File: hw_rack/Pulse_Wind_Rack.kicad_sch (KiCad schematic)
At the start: 12 parts, among them J1 PH2.00, J2 PH2.00, J3 AudioJack4, U1 ME6206A33XG

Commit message: fw: Rack board? To be revised
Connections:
- net GND: now also J1.1 (Pin_1); no longer J1.2 (Pin_2)
- net V+: now also J1.2 (Pin_2); no longer J1.1 (Pin_1)
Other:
- moved on the sheet: J2
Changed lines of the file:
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@@
 	(symbol
 		(lib_id "power:GND")
-		(at 48.26 38.1 90)
+		(at 48.26 35.56 90)
 		(unit 1)
 		(exclude_from_sim no)
@@
 		(fields_autoplaced yes)
 		(property "Reference" "#PWR02"
-			(at 54.61 38.1 0)
+			(at 54.61 35.56 0)
 			(effects
 				(font
@@
 		)
 		(property "Value" "GND"
-			(at 53.34 38.1 0)
+			(at 53.34 35.56 0)
 			(effects
 				(font
@@
 		)
 		(property "Footprint" ""
-			(at 48.26 38.1 0)
+			(at 48.26 35.56 0)
 			(effects
 				(font
@@
 		)
 		(property "Datasheet" ""
-			(at 48.26 38.1 0)
+			(at 48.26 35.56 0)
 			(effects
 				(font
@@
 		)
 		(property "Description" "Power symbol creates a global label with name \"GND\" , ground"
-			(at 48.26 38.1 0)
+			(at 48.26 35.56 0)
 			(effects
 				(font
@@
 	(symbol
 		(lib_id "Connector_Generic_MountingPin:Conn_01x02_MountingPin")
-		(at 69.85 35.56 0)
-		(unit 1)
-		(exclude_from_sim no)
-		(in_bom yes)
-		(on_board yes)
-		(dnp no)
-		(fields_autoplaced yes)
+		(at 69.85 38.1 0)
+		(mirror x)
+		(unit 1)
+		(exclude_from_sim no)
+		(in_bom yes)
+		(on_board yes)
+		(dnp no)
 		(property "Reference" "J2"
-			(at 69.85 29.21 0)
+			(at 69.85 44.45 0)
 			(effects
 				(font
@@
 		)
 		(property "Value" "PH2.00"
-			(at 69.85 31.75 0)
+			(at 69.85 41.91 0)
 			(effects
 				(font
@@
 		)
 		(property "Footprint" "Connector_JST:JST_PH_S2B-PH-SM4-TB_1x02-1MP_P2.00mm_Horizontal"
-			(at 69.85 35.56 0)
+			(at 69.85 38.1 0)
 			(effects
 				(font
@@
 		)
 		(property "Datasheet" "~"
-			(at 69.85 35.56 0)
+			(at 69.85 38.1 0)
 			(effects
 				(font
@@
 		)
 		(property "Description" "Generic connectable mounting pin connector, single row, 01x02, script generated (kicad-library-utils/schlib/autogen/connector/)"
-			(at 69.85 35.56 0)
+			(at 69.85 38.1 0)
 			(effects
 				(font
@@
 	(symbol
 		(lib_id "power:+BATT")
-		(at 64.77 35.56 90)
+		(at 64.77 38.1 90)
 		(mirror x)
 		(unit 1)
@@
 		(fields_autoplaced yes)
 		(property "Reference" "#PWR05"
-			(at 68.58 35.56 0)
+			(at 68.58 38.1 0)
 			(effects
 				(font
@@
 		)
 		(property "Value" "V+"
-			(at 60.96 35.5599 90)
+			(at 60.96 38.0999 90)
 			(effects
 				(font
@@
 		)
 		(property "Footprint" ""
-			(at 64.77 35.56 0)
+			(at 64.77 38.1 0)
 			(effects
 				(font
@@
 		)
 		(property "Datasheet" ""
-			(at 64.77 35.56 0)
+			(at 64.77 38.1 0)
 			(effects
 				(font
@@
 		)
 		(property "Description" "Power symbol creates a global label with name \"+BATT\""
-			(at 64.77 35.56 0)
+			(at 64.77 38.1 0)
 			(effects
 				(font
@@
 	(symbol
 		(lib_id "power:GND")
-		(at 64.77 38.1 270)
+		(at 64.77 35.56 270)
 		(mirror x)
 		(unit 1)
@@
 		(fields_autoplaced yes)
 		(property "Reference" "#PWR06"
-			(at 58.42 38.1 0)
+			(at 58.42 35.56 0)
 			(effects
 				(font
@@
 		)
 		(property "Value" "GND"
-			(at 59.69 38.1 0)
+			(at 59.69 35.56 0)
 			(effects
 				(font
@@
 		)
 		(property "Footprint" ""
-			(at 64.77 38.1 0)
+			(at 64.77 35.56 0)
 			(effects
 				(font
@@
 		)
 		(property "Datasheet" ""
-			(at 64.77 38.1 0)
+			(at 64.77 35.56 0)
 			(effects
 				(font
@@
 		)
 		(property "Description" "Power symbol creates a global label with name \"GND\" , ground"
-			(at 64.77 38.1 0)
+			(at 64.77 35.56 0)
 			(effects
 				(font
@@
 	(symbol
 		(lib_id "power:+BATT")
-		(at 48.26 35.56 270)
+		(at 48.26 38.1 270)
 		(unit 1)
 		(exclude_from_sim no)
@@
 		(fields_autoplaced yes)
 		(property "Reference" "#PWR03"
-			(at 44.45 35.56 0)
+			(at 44.45 38.1 0)
 			(effects
 				(font
@@
 		)
 		(property "Value" "V+"
-			(at 52.07 35.5599 90)
+			(at 52.07 38.0999 90)
 			(effects
 				(font
@@
 		)
 		(property "Footprint" ""
-			(at 48.26 35.56 0)
+			(at 48.26 38.1 0)
 			(effects
 				(font
@@
 		)
 		(property "Datasheet" ""
-			(at 48.26 35.56 0)
+			(at 48.26 38.1 0)
 			(effects
 				(font
@@
 		)
 		(property "Description" "Power symbol creates a global label with name \"+BATT\""
-			(at 48.26 35.56 0)
+			(at 48.26 38.1 0)
 			(effects
 				(font
@@
 	(symbol
 		(lib_id "power:GND")
-		(at 69.85 43.18 0)
-		(mirror y)
+		(at 69.85 30.48 0)
+		(mirror x)
 		(unit 1)
 		(exclude_from_sim no)
@@
 		(fields_autoplaced yes)
 		(property "Reference" "#PWR04"
-			(at 69.85 49.53 0)
+			(at 69.85 24.13 0)
 			(effects
 				(font
@@
 		)
 		(property "Value" "GND"
-			(at 69.85 48.26 0)
+			(at 69.85 25.4 0)
 			(effects
 				(font
@@
 		)
 		(property "Footprint" ""
-			(at 69.85 43.18 0)
+			(at 69.85 30.48 0)
 			(effects
 				(font
@@
 		)
 		(property "Datasheet" ""
-			(at 69.85 43.18 0)
+			(at 69.85 30.48 0)
 			(effects
 				(font
@@
 		)
 		(property "Description" "Power symbol creates a global label with name \"GND\" , ground"
-			(at 69.85 43.18 0)
-			(effects
-				(font
+			(at 69.85 30.48 0)
+			(effects
+				(font

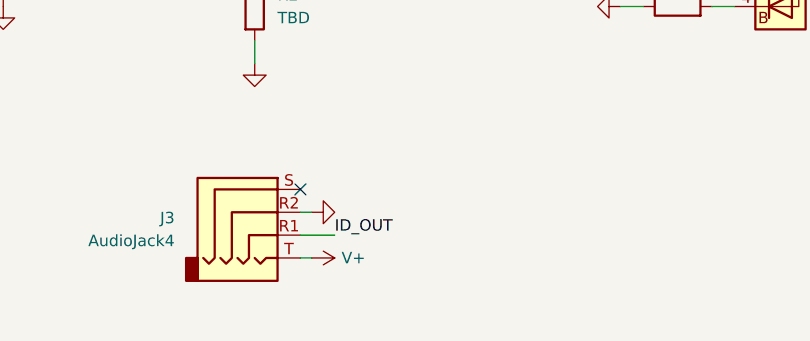
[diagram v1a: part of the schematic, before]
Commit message: hw: Add polyfuse in rack board
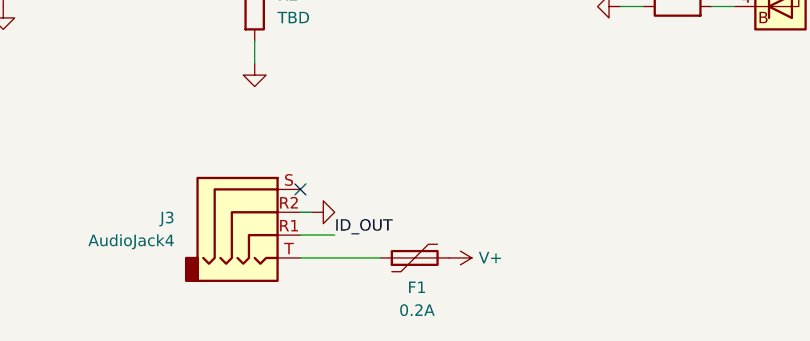
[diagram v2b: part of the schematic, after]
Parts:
- added F1: 0.2A, Fuse:Fuse_0603_1608Metric, symbol Device:Polyfuse
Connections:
- net V+: now also F1.2; no longer J3.T
- new net: F1.1, J3.T
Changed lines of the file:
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@@
 	(wire
 		(pts
-			(xy 106.68 101.6) (xy 105.41 101.6)
+			(xy 105.41 101.6) (xy 114.3 101.6)
 		)
 		(stroke
@@
 	)
 	(symbol
+		(lib_id "Device:Polyfuse")
+		(at 118.11 101.6 90)
+		(unit 1)
+		(exclude_from_sim no)
+		(in_bom yes)
+		(on_board yes)
+		(dnp no)
+		(property "Reference" "F1"
+			(at 118.364 104.902 90)
+			(effects
+				(font
+					(size 1.27 1.27)
+				)
+			)
+		)
+		(property "Value" "0.2A"
+			(at 118.364 107.442 90)
+			(effects
+				(font
+					(size 1.27 1.27)
+				)
+			)
+		)
+		(property "Footprint" "Fuse:Fuse_0603_1608Metric"
+			(at 123.19 100.33 0)
+			(effects
+				(font
+					(size 1.27 1.27)
+				)
+				(justify left)
+				(hide yes)
+			)
+		)
+		(property "Datasheet" "~"
+			(at 118.11 101.6 0)
+			(effects
+				(font
+					(size 1.27 1.27)
+				)
+				(hide yes)
+			)
+		)
+		(property "Description" "Resettable fuse, polymeric positive temperature coefficient"
+			(at 118.11 101.6 0)
+			(effects
+				(font
+					(size 1.27 1.27)
+				)
+				(hide yes)
+			)
+		)
+		(pin "2"
+		)
+		(pin "1"
+		)
+		(instances
+			(project ""
+				(path "/0b7ac699-7606-43e8-81ab-4a764f6cc88a"
+					(reference "F1")
+					(unit 1)
+				)
+			)
+		)
+	)
+	(symbol
 		(lib_id "Device:R")
 		(at 147.32 63.5 90)
@@
 	(symbol
 		(lib_id "power:+BATT")
-		(at 106.68 101.6 270)
+		(at 121.92 101.6 270)
 		(mirror x)
 		(unit 1)
@@
 		(dnp no)
 		(property "Reference" "#PWR013"
-			(at 102.87 101.6 0)
+			(at 118.11 101.6 0)
 			(effects
 				(font
@@
 		)
 		(property "Value" "V+"
-			(at 109.982 101.6 90)
+			(at 125.222 101.6 90)
 			(effects
 				(font
@@
 		)
 		(property "Footprint" ""
-			(at 106.68 101.6 0)
+			(at 121.92 101.6 0)
 			(effects
 				(font
@@
 		)
 		(property "Datasheet" ""
-			(at 106.68 101.6 0)
+			(at 121.92 101.6 0)
 			(effects
 				(font
@@
 		)
 		(property "Description" "Power symbol creates a global label with name \"+BATT\""
-			(at 106.68 101.6 0)
-			(effects
-				(font
+			(at 121.92 101.6 0)
+			(effects
+				(font
